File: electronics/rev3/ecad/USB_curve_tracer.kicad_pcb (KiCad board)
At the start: 2 copper layers, 117 x 64 mm, 66 parts, among them J1 DUT Connector, J2 Power Input, Q1 TIP122, Q2 TIP127, Q5 TIP122, Q6 TIP127, U1 MCP4911, U2 LMC6484IN, U3 MCP3204, U4 LM385BZ-2.5

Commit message: Layout work
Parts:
- removed Q5: TIP122, Package_TO_SOT_THT:TO-220-3_Vertical
- removed Q6: TIP127, Package_TO_SOT_THT:TO-220-3_Vertical
- added C10: 0.1uF, Capacitor_THT:C_Disc_D6.0mm_W2.5mm_P5.00mm, F.Cu at (161.7, 116.9)
- added C11: 100pF, Capacitor_THT:C_Disc_D6.0mm_W2.5mm_P5.00mm, F.Cu at (100.6, 92.4)
- added C6: 0.1uF, Capacitor_THT:C_Disc_D6.0mm_W2.5mm_P5.00mm, F.Cu at (118.3, 95.6)
- added C7: 10nF, Capacitor_THT:C_Disc_D6.0mm_W2.5mm_P5.00mm, F.Cu at (136.2, 82.0)
- added C9: 100pF, Capacitor_THT:C_Disc_D6.0mm_W2.5mm_P5.00mm, F.Cu at (105.6, 98.9)
- added D10: 1N4148, Diode_THT:D_DO-35_SOD27_P7.62mm_Horizontal, F.Cu at (138.0, 79.1)
- added D11: 1N4148, Diode_THT:D_DO-35_SOD27_P7.62mm_Horizontal, F.Cu at (137.9, 111.7)
- added D12: 1N4148, Diode_THT:D_DO-35_SOD27_P7.62mm_Horizontal, F.Cu at (100.1, 80.2)
- added D13: 1N4148, Diode_THT:D_DO-35_SOD27_P7.62mm_Horizontal, F.Cu at (107.7, 76.4)
- added D14: 1N4148, Diode_THT:D_DO-35_SOD27_P7.62mm_Horizontal, F.Cu at (100.4, 111.8)
- added D15: 1N4148, Diode_THT:D_DO-35_SOD27_P7.62mm_Horizontal, F.Cu at (108.0, 114.5)
- added D16: 1N5817, Diode_THT:D_DO-41_SOD81_P10.16mm_Horizontal, F.Cu at (91.7, 114.0)
- added D8: 1N4148, Diode_THT:D_DO-35_SOD27_P7.62mm_Horizontal, F.Cu at (145.8, 75.5)
- added D9: 1N4148, Diode_THT:D_DO-35_SOD27_P7.62mm_Horizontal, F.Cu at (145.5, 114.4)
- added HS1: 13.40°C/W, Library:HSINK_531002B02500G, F.Cu at (104.0, 64.3)
- added HS2: 13.40°C/W, Library:HSINK_531002B02500G, F.Cu at (104.0, 126.8)
- added HS3: 13.40°C/W, Library:HSINK_531002B02500G, F.Cu at (141.4, 64.3)
- added HS4: 13.40°C/W, Library:HSINK_531002B02500G, F.Cu at (141.4, 126.8)
- added Q3: TIP122, Package_TO_SOT_THT:TO-220-3_Vertical, F.Cu at (101.6, 69.3)
- added Q4: TIP127, Package_TO_SOT_THT:TO-220-3_Vertical, F.Cu at (106.8, 121.8)
- added R31: 4.7k, Resistor_THT:R_Axial_DIN0207_L6.3mm_D2.5mm_P7.62mm_Horizontal, F.Cu at (145.5, 118.4)
- added R32: 1k, Resistor_THT:R_Axial_DIN0207_L6.3mm_D2.5mm_P7.62mm_Horizontal, F.Cu at (110.8, 102.2)
- added R33: 10k, Resistor_THT:R_Axial_DIN0207_L6.3mm_D2.5mm_P7.62mm_Horizontal, F.Cu at (110.8, 98.9)
- added R34: 4.7k, Resistor_THT:R_Axial_DIN0207_L6.3mm_D2.5mm_P7.62mm_Horizontal, F.Cu at (107.7, 73.4)
- added R35: 4.7k, Resistor_THT:R_Axial_DIN0207_L6.3mm_D2.5mm_P7.62mm_Horizontal, F.Cu at (108.0, 118.5)
- added R36: 1.5, Resistor_SMD:R_2512_6332Metric_Pad1.40x3.35mm_HandSolder, F.Cu at (100.3, 85.9)
- added R37: 1+/-1%, Resistor_SMD:R_2512_6332Metric_Pad1.40x3.35mm_HandSolder, F.Cu at (144.9, 94.0)
- C8: value 0.1uF -> 10nF
- F1: value 2A -> 3A
- R10, R19: value 250k+/-0.1% -> 11.8k+/-0.1%
- R13: value 0.1+/-0.1% -> 1+/-1%; footprint Resistor_THT:R_Axial_DIN0207_L6.3mm_D2.5mm_P7.62mm_Horizontal -> Resistor_SMD:R_2512_6332Metric_Pad1.40x3.35mm_HandSolder
- R18, R8: value 10k+/-0.1% -> 1k+/-0.1%
- R20, R28: value 1k -> 1k+/-0.1%
- R23: value 3240 -> 3.83k+/-0.1%
- R29, R5: value 4.7k -> 3.83k+/-0.1%
- R4: value 1k -> 4.7k
- TP5, TP6: value TestPoint -> 4952
- U2: value LMC6484IN -> LMC6484A
- moved H3 136.2 mm to (205.0, 61.0)
- moved H2 130.1 mm to (79.0, 130.0)
- moved TP5 58.8 mm to (96.5, 75.8)
- moved TP6 55.2 mm to (121.6, 84.0)
- moved Q2 48.8 mm to (143.8, 121.8), turned to 180 degrees
- moved R24 42.7 mm to (179.1, 117.6), turned to 180 degrees
- moved R1 40.8 mm to (154.1, 75.6)
- moved R25 40.6 mm to (179.1, 114.3), turned to 180 degrees
- moved R26 39.1 mm to (179.1, 111.1), turned to 180 degrees
- moved U1 38.2 mm to (171.6, 72.1)
- moved R27 38.0 mm to (179.1, 107.9), turned to 180 degrees
- moved U4 34.1 mm to (167.1, 120.1), turned to -90 degrees
- moved TP4 31.7 mm to (166.8, 95.8)
- moved TP1 31.5 mm to (94.5, 90.6)
- moved D4 31.1 mm to (161.8, 91.4), turned to 180 degrees
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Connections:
- net /IV_Variation/DUT- renamed Net-(D2-A1)
- net /IV_Variation/VADJ renamed /IV_Variation/Sweep_Input
- C4 pad 1: +12V -> Net-(U2B-+)
- C8 pad 1: Net-(U2B-+) -> Net-(U2C--)
- C8 pad 2: GND -> Net-(C8-Pad2)
- D2 pad 2: /IV_Variation/DUT+ -> Net-(D2-A2)
- F1 pad 2: +12V -> Net-(D16-A)
- J1 pad 2: /IV_Variation/DUT+ -> Net-(D2-A2)
- Q1 pad 1: Net-(Q1-B) -> Net-(D8-A)
- Q2 pad 1: Net-(Q1-B) -> Net-(D9-K)
- R14 pad 2: Net-(R14-Pad2) -> Net-(C8-Pad2)
- R16 pad 1: /IV_Variation/DUT+ -> Net-(D2-A2)
- R4 pad 1: Net-(R4-Pad1) -> +12V
- R4 pad 2: Net-(Q1-B) -> Net-(D8-A)
- R5 pad 1: Net-(R14-Pad2) -> Net-(C8-Pad2)
- R6 pad 2: /IV_Variation/DUT+ -> GND
- R7 pad 2: GND -> /IV_Variation/Sweep Voltage Buffer/Sweep_Amplified
- R9 pad 2: Net-(Q5-B) -> /IV_Variation/Sweep Voltage Buffer/Sweep_Amplified
- TP1 pad 1: /IV_Variation/DUT+ -> Net-(D2-A2)
- U2 pad 6: V/2 -> Net-(U2B--)
- U2 pad 7: Net-(R4-Pad1) -> Net-(D10-K)
- U2 pad 8: Net-(R14-Pad2) -> Net-(C8-Pad2)
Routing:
- net +12V: track 176.2 -> 0.00 mm, vias 2 -> 0
- net /IV_Variation/DUT+: track 125.8 -> 0.00 mm, vias 2 -> 0
- net /IV_Variation/Sweep_Input: track 81.3 -> 12.3 mm, vias 8 -> 0
- net Net-(A1-D10): track 67.4 -> 0.00 mm, vias 2 -> 0
- net Net-(D2-A1): track 101.0 -> 39.0 mm, vias 7 -> 0
- net Net-(C7-Pad2): track 58.7 -> 3.20 mm, vias 2 -> 0
- net Net-(R14-Pad2): track 54.4 -> 0.00 mm, vias 3 -> 0
- net /IV_Variation/Sweep Voltage Buffer/Sweep_Amplified: track 0.00 -> 51.6 mm
- net Net-(A1-D8): track 50.4 -> 0.00 mm
- net Net-(A1-D11): track 56.3 -> 10.8 mm
- net Net-(A1-D7): track 41.8 -> 0.00 mm
- net Net-(A1-D6): track 51.9 -> 11.8 mm
- net V/2: track 126.0 -> 86.8 mm, vias 2 -> 0
- net Net-(A1-D12): track 37.0 -> 0.00 mm
- net Net-(A1-D9): track 34.5 -> 0.00 mm
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- added copper zone on F.Cu, net +12V
- removed copper zone on F.Cu, net +5V
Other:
- board size 117 x 64 mm -> 134 x 77 mm
- board text removed: "12V"
- board text removed: "Curve Tracer"
- board text removed: "DUT+"
- board text removed: "DUT-"
- board text removed: "GND"
- board text removed: "MN"
- board text removed: "REV2"

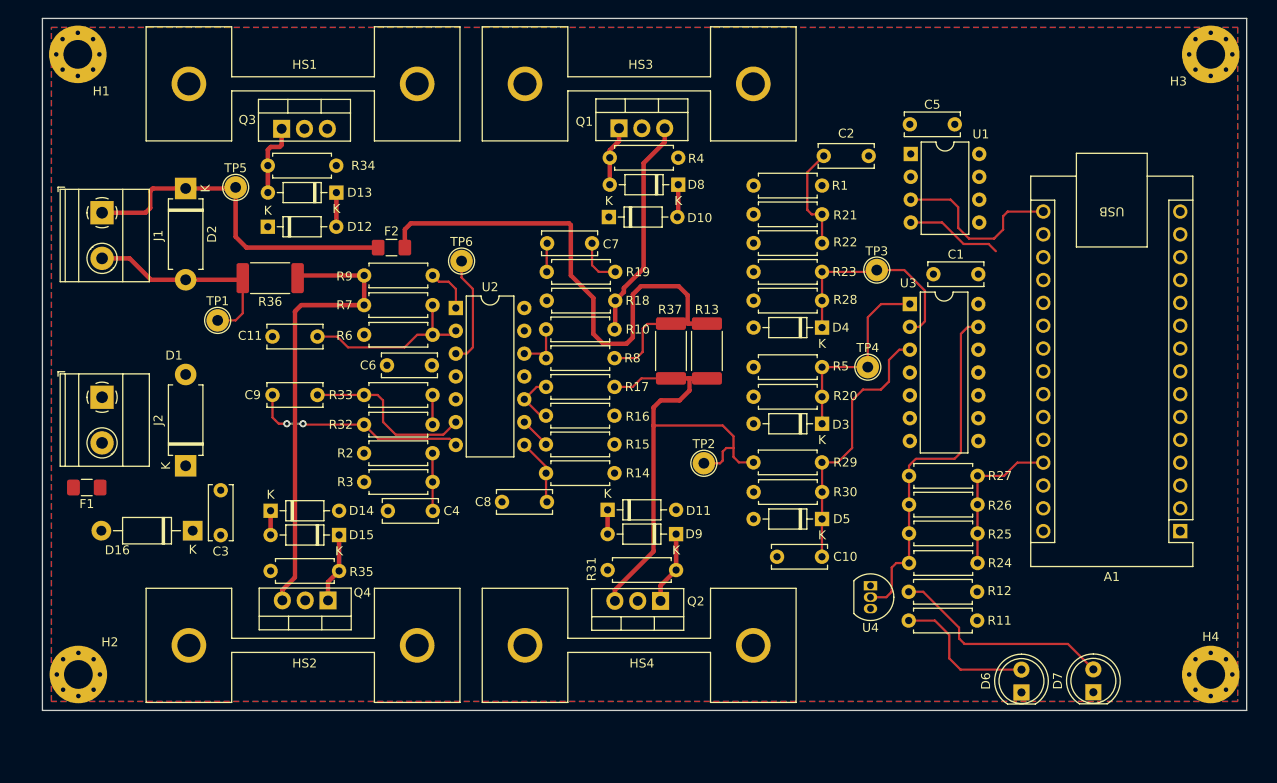
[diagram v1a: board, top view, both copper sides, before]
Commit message: start direction modes
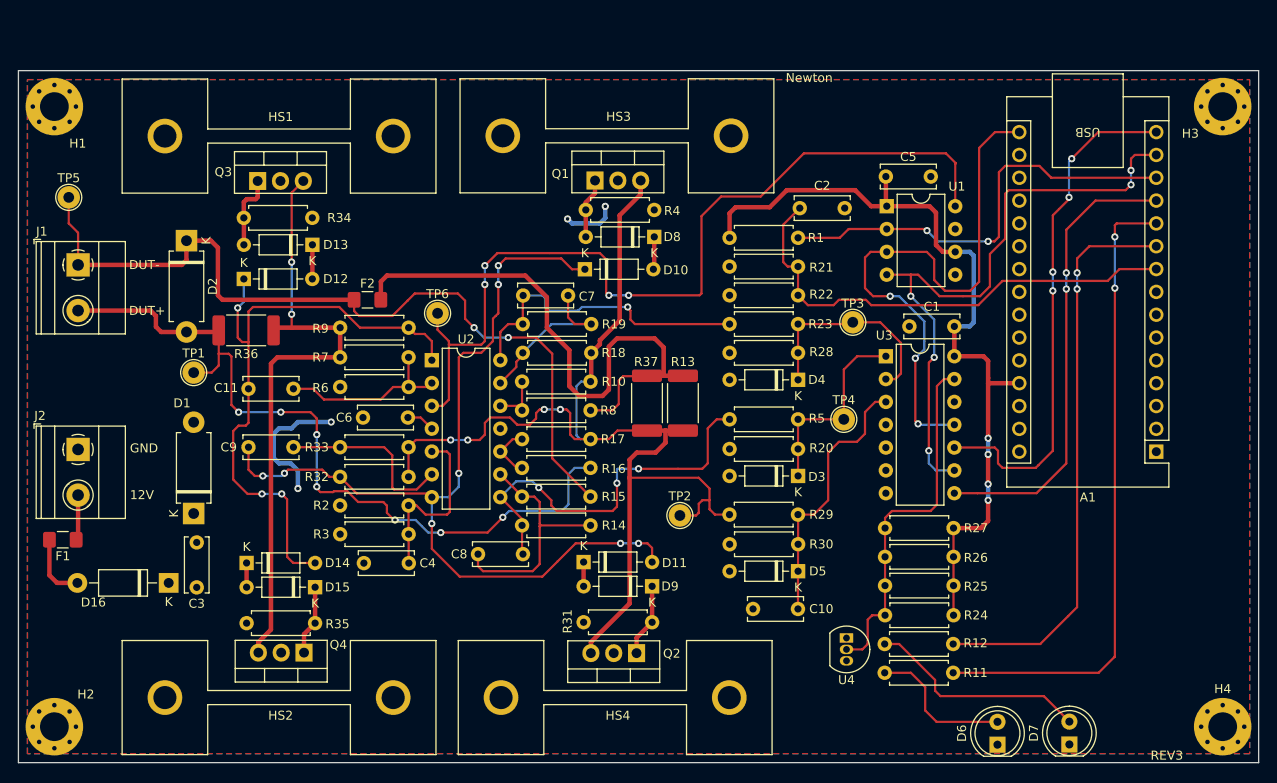
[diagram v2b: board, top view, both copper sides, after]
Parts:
- moved TP5 18.6 mm to (77.9, 76.9)
- moved A1 9.23 mm to (198.9, 105.2)
- moved C5 6.39 mm to (168.8, 74.6)
- moved R16 6.39 mm to (136.0, 107.0)
- moved R19 6.39 mm to (136.1, 91.0)
- moved R24 6.39 mm to (176.4, 123.4)
- moved R25 6.39 mm to (176.4, 120.1)
- moved R26 6.39 mm to (176.4, 116.9)
- moved TP3 6.39 mm to (165.2, 90.8)
- moved TP4 6.39 mm to (164.2, 101.6)
- moved U1 6.39 mm to (168.9, 77.9)
- moved U3 6.39 mm to (168.8, 94.6)
- moved C3 6.39 mm to (92.2, 120.3)
- moved C4 6.39 mm to (115.8, 117.6)
- moved C6 6.39 mm to (115.7, 101.4)
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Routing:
- net /IV_Variation/Sweep_Input: track 12.3 -> 98.8 mm, vias 0 -> 4
- net Net-(D10-K): track 24.2 -> 101.1 mm, vias 2 -> 8
- net +5V: track 17.6 -> 91.6 mm, vias 0 -> 4
- net Net-(A1-D8): track 0.00 -> 71.4 mm, vias 0 -> 2
- net Net-(D12-K): track 5.32 -> 69.1 mm, vias 0 -> 3
- net Net-(A1-D7): track 0.00 -> 63.7 mm, vias 0 -> 2
- net Net-(D2-A2): track 23.7 -> 87.3 mm, vias 0 -> 7
- net Net-(A1-D11): track 10.8 -> 69.7 mm, vias 0 -> 5
- net Net-(A1-D12): track 0.00 -> 57.5 mm, vias 0 -> 4
- net Net-(D2-A1): track 39.0 -> 93.1 mm, vias 0 -> 2
- net Net-(A1-D9): track 0.00 -> 51.2 mm, vias 0 -> 2
- net Net-(A1-D10): track 0.00 -> 49.1 mm, vias 0 -> 2
- net Net-(A1-D13): track 20.0 -> 64.2 mm, vias 0 -> 3
- net Net-(A1-D6): track 11.8 -> 54.3 mm
- net Net-(C8-Pad2): track 7.38 -> 44.3 mm, vias 0 -> 3
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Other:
- board size 134 x 77 mm -> 138 x 77 mm
- board text added: "12V"
- board text added: "DUT+"
- board text added: "DUT-"
- board text added: "GND"
- board text added: "Newton"
- board text added: "REV3"
